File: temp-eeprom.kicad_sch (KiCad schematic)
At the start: 12 parts, among them U5 MCP9804_MSOP, U6 M24C02-WMN

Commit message: Add LCSC order numbers to more easily order at JLCPCB
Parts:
- C38, C39: LCSC Part # (none) -> C14663
- R32, R33, R34, R35: LCSC Part # (none) -> C25804
- U6: LCSC Part # (none) -> C7562
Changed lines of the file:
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@@
   (symbol (lib_id "power:GND") (at 55.88 39.37 0) (unit 1)
     (in_bom yes) (on_board yes) (fields_autoplaced)
-    (property "Reference" "#PWR?" (id 0) (at 55.88 45.72 0)
+    (property "Reference" "#PWR0122" (id 0) (at 55.88 45.72 0)
       (effects (font (size 1.27 1.27)) hide)
     )
@@
   (symbol (lib_id "power:+5V") (at 55.88 69.9765 0) (unit 1)
     (in_bom yes) (on_board yes) (fields_autoplaced)
-    (property "Reference" "#PWR?" (id 0) (at 55.88 73.7865 0)
+    (property "Reference" "#PWR0107" (id 0) (at 55.88 73.7865 0)
       (effects (font (size 1.27 1.27)) hide)
     )
@@
   (symbol (lib_id "power:GND") (at 55.88 105.5365 0) (unit 1)
     (in_bom yes) (on_board yes) (fields_autoplaced)
-    (property "Reference" "#PWR?" (id 0) (at 55.88 111.8865 0)
+    (property "Reference" "#PWR0108" (id 0) (at 55.88 111.8865 0)
       (effects (font (size 1.27 1.27)) hide)
     )
@@
       (effects (font (size 1.27 1.27)) hide)
     )
+    (property "LCSC Part #" "C14663" (id 4) (at 55.88 33.02 0)
+      (effects (font (size 1.27 1.27)) hide)
+    )
     (pin "1")
     (pin "2")
@@
   (symbol (lib_id "power:+5V") (at 151.13 107.95 0) (unit 1)
     (in_bom yes) (on_board yes) (fields_autoplaced)
-    (property "Reference" "#PWR?" (id 0) (at 151.13 111.76 0)
+    (property "Reference" "#PWR0104" (id 0) (at 151.13 111.76 0)
       (effects (font (size 1.27 1.27)) hide)
     )
@@
   (symbol (lib_id "power:GND") (at 38.1 105.41 0) (unit 1)
     (in_bom yes) (on_board yes) (fields_autoplaced)
-    (property "Reference" "#PWR?" (id 0) (at 38.1 111.76 0)
+    (property "Reference" "#PWR0110" (id 0) (at 38.1 111.76 0)
       (effects (font (size 1.27 1.27)) hide)
     )
@@
   (symbol (lib_id "power:+5V") (at 55.88 26.67 0) (unit 1)
     (in_bom yes) (on_board yes) (fields_autoplaced)
-    (property "Reference" "#PWR?" (id 0) (at 55.88 30.48 0)
+    (property "Reference" "#PWR0119" (id 0) (at 55.88 30.48 0)
       (effects (font (size 1.27 1.27)) hide)
     )
@@
       (effects (font (size 1.27 1.27)) hide)
     )
+    (property "LCSC Part #" "C25804" (id 4) (at 180.34 137.16 0)
+      (effects (font (size 1.27 1.27)) hide)
+    )
     (pin "1")
     (pin "2")
@@
   (symbol (lib_id "power:+5V") (at 41.91 26.67 0) (unit 1)
     (in_bom yes) (on_board yes) (fields_autoplaced)
-    (property "Reference" "#PWR?" (id 0) (at 41.91 30.48 0)
+    (property "Reference" "#PWR0120" (id 0) (at 41.91 30.48 0)
       (effects (font (size 1.27 1.27)) hide)
     )
@@
     )
     (property "Datasheet" "http://www.st.com/content/ccc/resource/technical/document/datasheet/b0/d8/50/40/5a/85/49/6f/DM00071904.pdf/files/DM00071904.pdf/jcr:content/translations/en.DM00071904.pdf" (id 3) (at 152.4 130.81 0)
+      (effects (font (size 1.27 1.27)) hide)
+    )
+    (property "LCSC Part #" "C7562" (id 4) (at 151.13 118.11 0)
       (effects (font (size 1.27 1.27)) hide)
     )
@@
   (symbol (lib_id "power:+5V") (at 151.13 54.61 0) (unit 1)
     (in_bom yes) (on_board yes) (fields_autoplaced)
-    (property "Reference" "#PWR?" (id 0) (at 151.13 58.42 0)
+    (property "Reference" "#PWR0103" (id 0) (at 151.13 58.42 0)
       (effects (font (size 1.27 1.27)) hide)
     )
@@
       (effects (font (size 1.27 1.27)) hide)
     )
+    (property "LCSC Part #" "C25804" (id 4) (at 55.88 99.1865 0)
+      (effects (font (size 1.27 1.27)) hide)
+    )
     (pin "1")
     (pin "2")
@@
   (symbol (lib_id "power:+5V") (at 46.99 69.85 0) (unit 1)
     (in_bom yes) (on_board yes) (fields_autoplaced)
-    (property "Reference" "#PWR?" (id 0) (at 46.99 73.66 0)
+    (property "Reference" "#PWR0111" (id 0) (at 46.99 73.66 0)
       (effects (font (size 1.27 1.27)) hide)
     )
@@
   (symbol (lib_id "power:GND") (at 151.13 128.27 0) (unit 1)
     (in_bom yes) (on_board yes) (fields_autoplaced)
-    (property "Reference" "#PWR?" (id 0) (at 151.13 134.62 0)
+    (property "Reference" "#PWR0102" (id 0) (at 151.13 134.62 0)
       (effects (font (size 1.27 1.27)) hide)
     )
@@
       (effects (font (size 1.27 1.27)) hide)
     )
+    (property "LCSC Part #" "C25804" (id 4) (at 46.99 99.06 0)
+      (effects (font (size 1.27 1.27)) hide)
+    )
     (pin "1")
     (pin "2")
@@
   (symbol (lib_id "power:GND") (at 180.34 143.51 0) (unit 1)
     (in_bom yes) (on_board yes) (fields_autoplaced)
-    (property "Reference" "#PWR?" (id 0) (at 180.34 149.86 0)
+    (property "Reference" "#PWR0101" (id 0) (at 180.34 149.86 0)
       (effects (font (size 1.27 1.27)) hide)
     )
@@
       (effects (font (size 1.27 1.27)) hide)
     )
+    (property "LCSC Part #" "C25804" (id 4) (at 38.1 99.06 0)
+      (effects (font (size 1.27 1.27)) hide)
+    )
     (pin "1")
     (pin "2")
@@
   (symbol (lib_id "power:GND") (at 151.13 85.09 0) (unit 1)
     (in_bom yes) (on_board yes) (fields_autoplaced)
-    (property "Reference" "#PWR?" (id 0) (at 151.13 91.44 0)
+    (property "Reference" "#PWR0105" (id 0) (at 151.13 91.44 0)
       (effects (font (size 1.27 1.27)) hide)
     )
@@
   (symbol (lib_id "power:+5V") (at 38.1 69.85 0) (unit 1)
     (in_bom yes) (on_board yes) (fields_autoplaced)
-    (property "Reference" "#PWR?" (id 0) (at 38.1 73.66 0)
+    (property "Reference" "#PWR0112" (id 0) (at 38.1 73.66 0)
       (effects (font (size 1.27 1.27)) hide)
     )
@@
   (symbol (lib_id "power:GND") (at 46.99 105.41 0) (unit 1)
     (in_bom yes) (on_board yes) (fields_autoplaced)
-    (property "Reference" "#PWR?" (id 0) (at 46.99 111.76 0)
+    (property "Reference" "#PWR0109" (id 0) (at 46.99 111.76 0)
       (effects (font (size 1.27 1.27)) hide)
     )
@@
       (effects (font (size 1.27 1.27)) hide)
     )
+    (property "LCSC Part #" "C14663" (id 4) (at 41.91 33.02 0)
+      (effects (font (size 1.27 1.27)) hide)
+    )
     (pin "1")
     (pin "2")
@@
   (symbol (lib_id "power:GND") (at 41.91 39.37 0) (unit 1)
     (in_bom yes) (on_board yes) (fields_autoplaced)
-    (property "Reference" "#PWR?" (id 0) (at 41.91 45.72 0)
+    (property "Reference" "#PWR0121" (id 0) (at 41.91 45.72 0)
       (effects (font (size 1.27 1.27)) hide)
     )
@@
   (symbol (lib_id "power:+5V") (at 180.34 107.95 0) (unit 1)
     (in_bom yes) (on_board yes) (fields_autoplaced)
-    (property "Reference" "#PWR?" (id 0) (at 180.34 111.76 0)
-      (effects (font (size 1.27 1.27)) hide)
-    )
+    (property "Reference" "#PWR0106" (id 0) (at 180.34 111.76 0)
+      (effects (font (size 1.27 1.27)) hide)
+    )

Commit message: Remove PCB only parts from BOM
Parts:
- JP10, JP17, JP8, JP9: now left out of the parts list
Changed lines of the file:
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@@
   )
   (symbol (lib_id "Jumper:SolderJumper_2_Open") (at 38.1 76.2 90) (unit 1)
-    (in_bom yes) (on_board yes) (fields_autoplaced)
+    (in_bom no) (on_board yes) (fields_autoplaced)
     (property "Reference" "JP8" (id 0) (at 40.64 76.1999 90)
       (effects (font (size 1.27 1.27)) (justify right))
@@
   )
   (symbol (lib_id "Jumper:SolderJumper_2_Open") (at 55.88 76.3265 90) (unit 1)
-    (in_bom yes) (on_board yes) (fields_autoplaced)
+    (in_bom no) (on_board yes) (fields_autoplaced)
     (property "Reference" "JP17" (id 0) (at 58.42 76.3264 90)
       (effects (font (size 1.27 1.27)) (justify right))
@@
   )
   (symbol (lib_id "Jumper:SolderJumper_2_Open") (at 180.34 114.3 90) (unit 1)
-    (in_bom yes) (on_board yes) (fields_autoplaced)
+    (in_bom no) (on_board yes) (fields_autoplaced)
     (property "Reference" "JP10" (id 0) (at 182.88 114.2999 90)
       (effects (font (size 1.27 1.27)) (justify right))
@@
   )
   (symbol (lib_id "Jumper:SolderJumper_2_Open") (at 46.99 76.2 90) (unit 1)
-    (in_bom yes) (on_board yes) (fields_autoplaced)
+    (in_bom no) (on_board yes) (fields_autoplaced)
     (property "Reference" "JP9" (id 0) (at 49.53 76.1999 90)
       (effects (font (size 1.27 1.27)) (justify right))

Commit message: Add JLCPCB rotation offsets
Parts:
- U6: JLCPCB Rotation Offset (none) -> -90
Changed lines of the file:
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@@
+      (effects (font (size 1.27 1.27)) hide)
+    )
+    (property "JLCPCB Rotation Offset" "-90" (id 5) (at 151.13 118.11 0)
       (effects (font (size 1.27 1.27)) hide)
     )

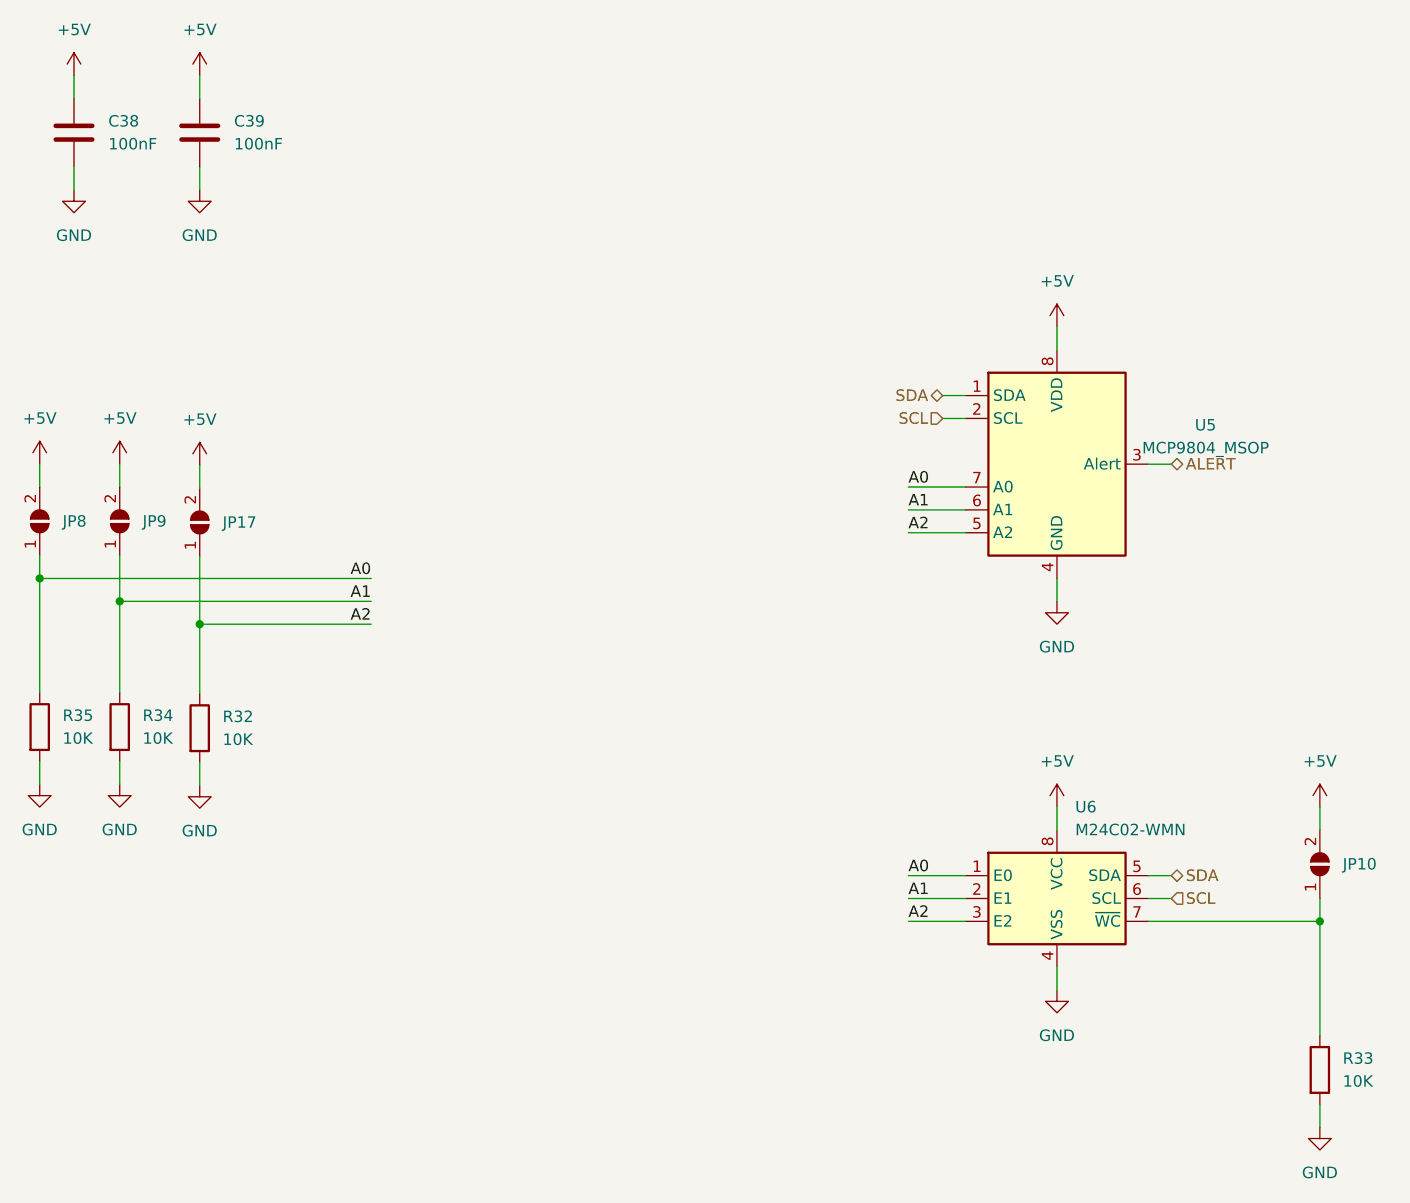
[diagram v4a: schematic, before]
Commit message: Shrink board and reduce features to reduce price
* Shrink to 100mm x 50mm
* Remove voltage regulator and use Stemma Power instead
* Remove isolation (is easier to add outside when needed)
* Remove reverse indicators to save space
* Remove I2C pullups as they are no longer needed
* Fix A2 of EEPROM and Temperature sensor to 0 to save space
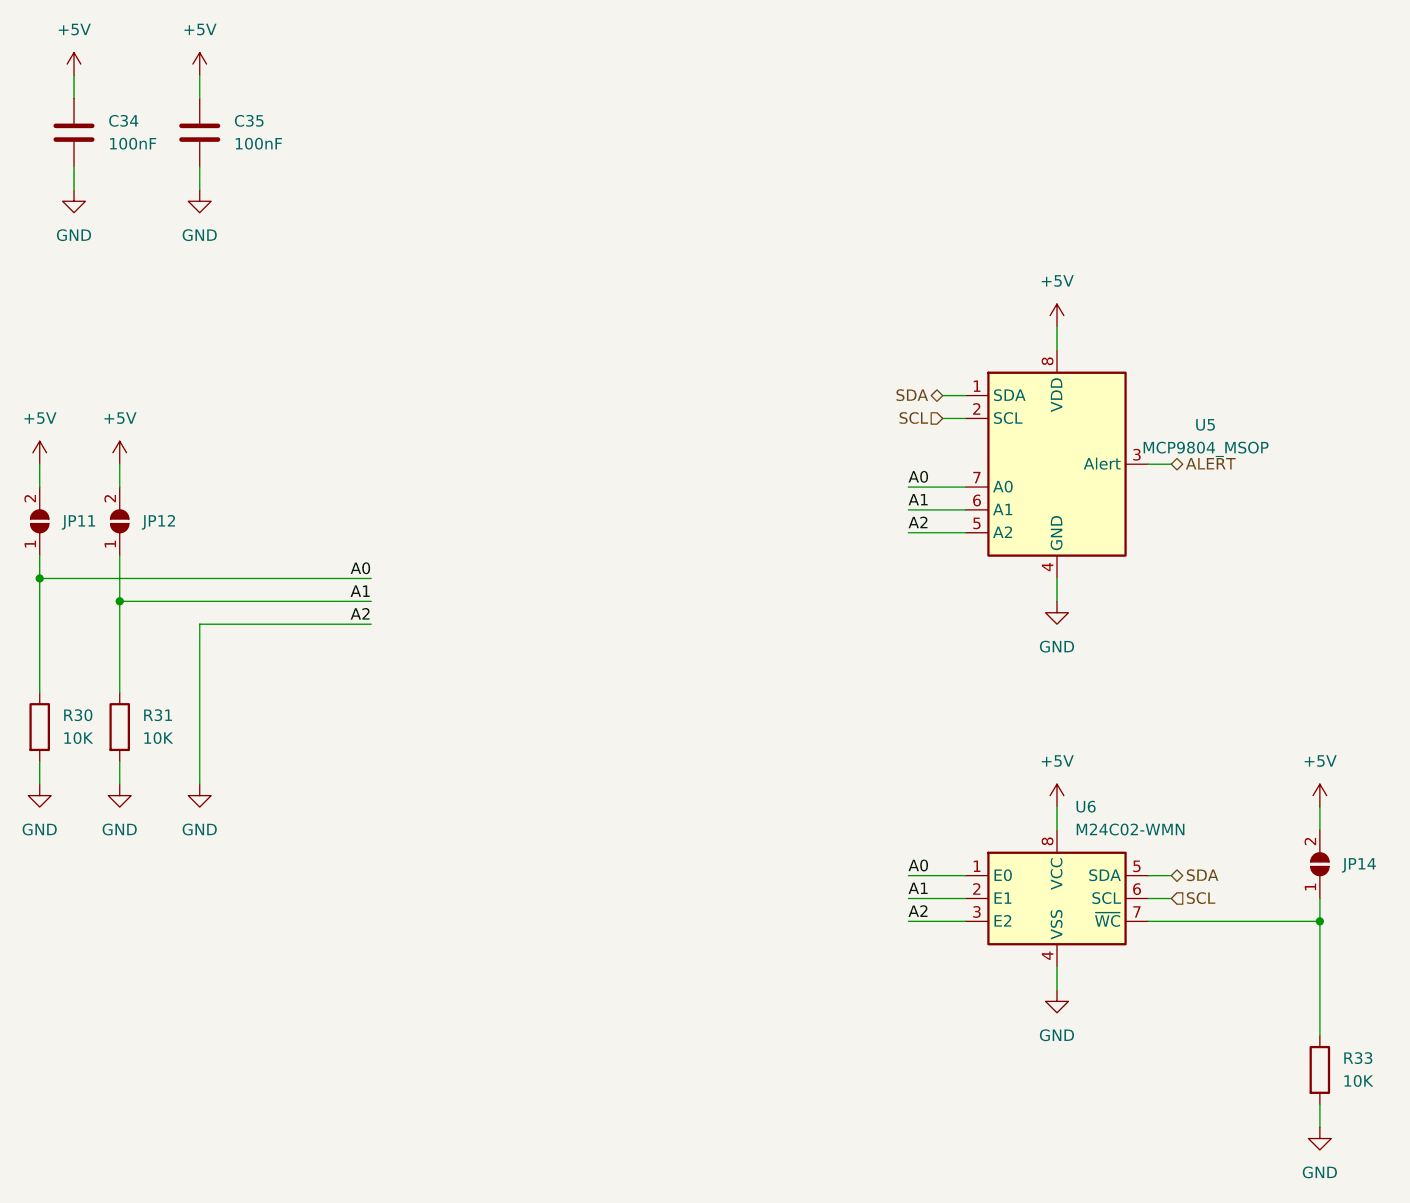
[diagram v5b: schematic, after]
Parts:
- removed JP17: SolderJumper_2_Open, Jumper:SolderJumper-2_P1.3mm_Open_TrianglePad1.0x1.5mm, symbol Jumper:SolderJumper_2_Open
- removed R32: 10K, Resistor_SMD:R_0603_1608Metric, symbol Device:R
- renumbered C38 to C34, C39 to C35, JP8 to JP11, JP9 to JP12, JP10 to JP14, R35 to R30, R34 to R31
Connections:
- net A2 is gone; now on net GND: U5.5 (A2), U6.3 (E2)

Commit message: Switch shunt footprint
The 2816 footprint is big enough to also mount all the smaller
resistors down to 1206 and allows munting the bigger 2816
resistors.
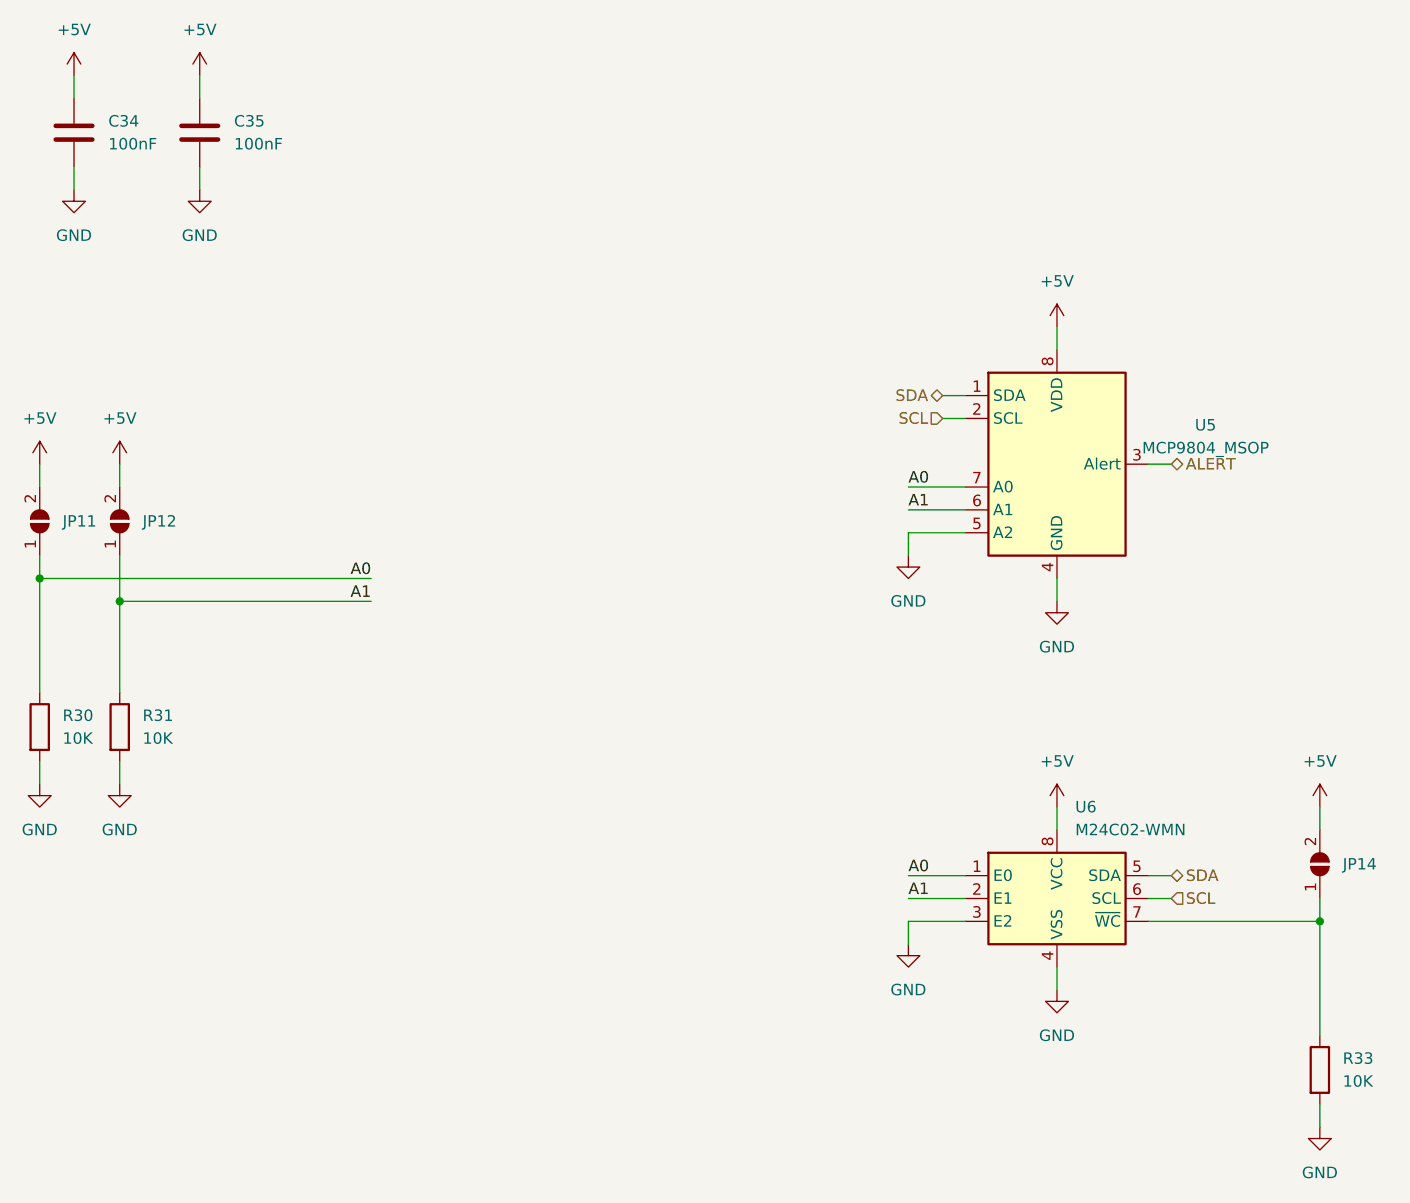
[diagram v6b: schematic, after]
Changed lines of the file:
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@@
-    (stroke (width 0) (type default) (color 0 0 0 0))
-  )
-  (wire (pts (xy 55.88 87.63) (xy 55.88 105.41))
     (stroke (width 0) (type default) (color 0 0 0 0))
   )
@@
     (stroke (width 0) (type default) (color 0 0 0 0))
   )
-  (wire (pts (xy 55.88 87.63) (xy 74.93 87.63))
+  (wire (pts (xy 134.62 120.65) (xy 134.62 123.19))
     (stroke (width 0) (type default) (color 0 0 0 0))
   )
@@
     (stroke (width 0) (type default) (color 0 0 0 0))
   )
+  (wire (pts (xy 134.62 77.47) (xy 134.62 80.01))
+    (stroke (width 0) (type default) (color 0 0 0 0))
+  )
   (wire (pts (xy 38.1 80.01) (xy 38.1 82.55))
     (stroke (width 0) (type default) (color 0 0 0 0))
@@
   (wire (pts (xy 138.43 62.23) (xy 140.97 62.23))
     (stroke (width 0) (type default) (color 0 0 0 0))
-  )
-  (label "A2" (at 74.93 87.63 180)
-    (effects (font (size 1.27 1.27)) (justify right bottom))
   )
   (label "A1" (at 134.62 118.11 0)
@@
     (effects (font (size 1.27 1.27)) (justify right bottom))
   )
-  (label "A2" (at 134.62 120.65 0)
-    (effects (font (size 1.27 1.27)) (justify left bottom))
-  )
   (label "A0" (at 134.62 115.57 0)
     (effects (font (size 1.27 1.27)) (justify left bottom))
@@
     (effects (font (size 1.27 1.27)) (justify left bottom))
   )
-  (label "A2" (at 134.62 77.47 0)
-    (effects (font (size 1.27 1.27)) (justify left bottom))
-  )
   (label "A1" (at 134.62 74.93 0)
     (effects (font (size 1.27 1.27)) (justify left bottom))
@@
     )
     (property "Datasheet" "" (id 3) (at 55.88 39.37 0)
-      (effects (font (size 1.27 1.27)) hide)
-    )
-    (pin "1")
-  )
-  (symbol (lib_id "power:GND") (at 55.88 105.41 0) (unit 1)
-    (in_bom yes) (on_board yes) (fields_autoplaced)
-    (property "Reference" "#PWR096" (id 0) (at 55.88 111.76 0)
-      (effects (font (size 1.27 1.27)) hide)
-    )
-    (property "Value" "GND" (id 1) (at 55.88 110.49 0))
-    (property "Footprint" "" (id 2) (at 55.88 105.41 0)
-      (effects (font (size 1.27 1.27)) hide)
-    )
-    (property "Datasheet" "" (id 3) (at 55.88 105.41 0)
       (effects (font (size 1.27 1.27)) hide)
     )
@@
     (pin "2")
   )
+  (symbol (lib_id "power:GND") (at 134.62 123.19 0) (unit 1)
+    (in_bom yes) (on_board yes) (fields_autoplaced)
+    (property "Reference" "#PWR0110" (id 0) (at 134.62 129.54 0)
+      (effects (font (size 1.27 1.27)) hide)
+    )
+    (property "Value" "GND" (id 1) (at 134.62 128.27 0))
+    (property "Footprint" "" (id 2) (at 134.62 123.19 0)
+      (effects (font (size 1.27 1.27)) hide)
+    )
+    (property "Datasheet" "" (id 3) (at 134.62 123.19 0)
+      (effects (font (size 1.27 1.27)) hide)
+    )
+    (pin "1")
+  )
   (symbol (lib_id "power:GND") (at 38.1 105.41 0) (unit 1)
     (in_bom yes) (on_board yes) (fields_autoplaced)
@@
       (effects (font (size 1.27 1.27)) hide)
     )
+    (pin "1")
+  )
+  (symbol (lib_id "power:GND") (at 134.62 80.01 0) (unit 1)
+    (in_bom yes) (on_board yes) (fields_autoplaced)
+    (property "Reference" "#PWR0109" (id 0) (at 134.62 86.36 0)
+      (effects (font (size 1.27 1.27)) hide)
+    )
+    (property "Value" "GND" (id 1) (at 134.62 85.09 0))
+    (property "Footprint" "" (id 2) (at 134.62 80.01 0)
+      (effects (font (size 1.27 1.27)) hide)
+    )
+    (property "Datasheet" "" (id 3) (at 134.62 80.01 0)
+      (effects (font (size 1.27 1.27)) hide)
+    )
